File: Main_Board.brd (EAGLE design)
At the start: 160 x 100 mm, 50 parts, among them U1 RN4020RN4020, Y1 32KHz, Y2 25MHz

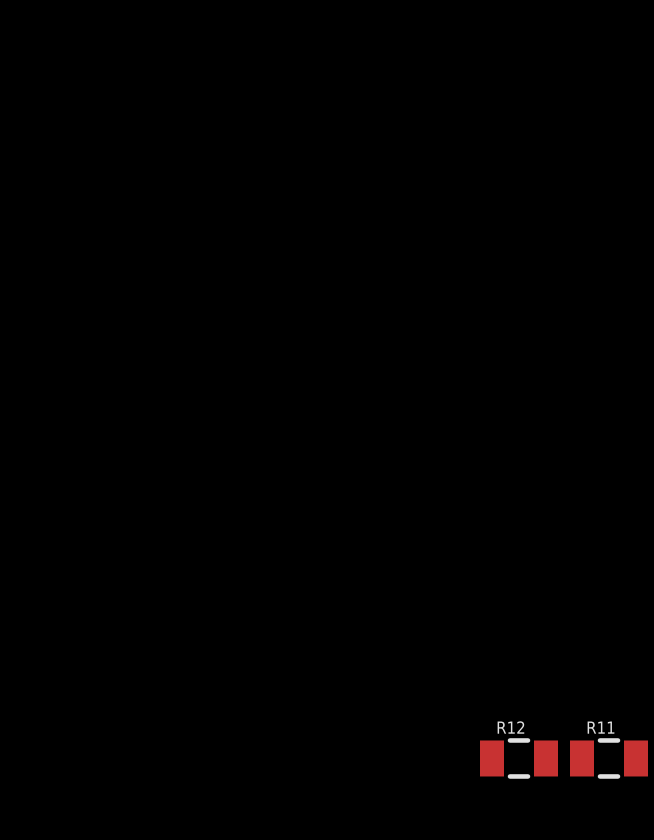
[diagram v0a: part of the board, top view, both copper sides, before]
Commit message: Added most remaining STM requirements
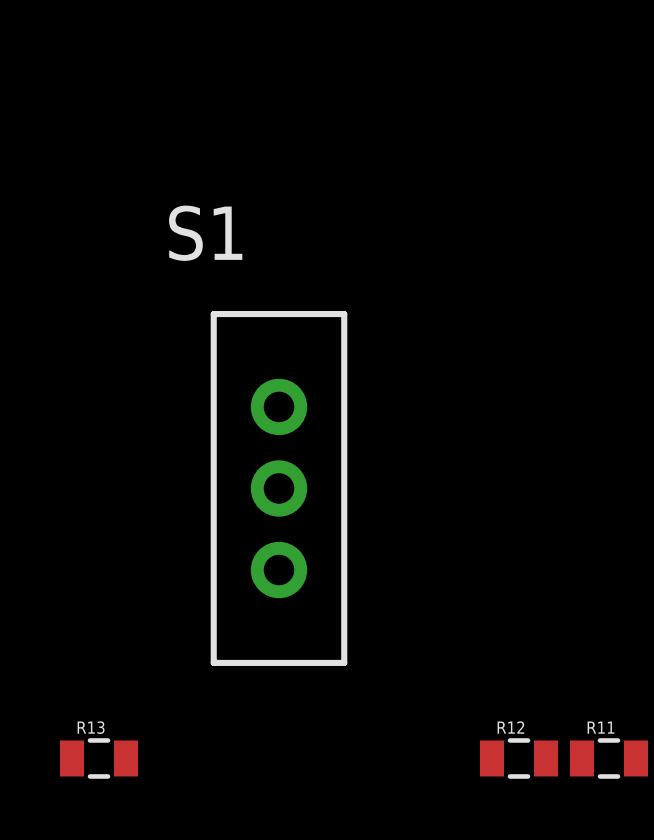
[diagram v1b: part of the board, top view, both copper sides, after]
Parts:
- added R13: 10K, SparkFun-Passives:0805
- added S1: (no value), SparkFun-Electromechanical:SWITCH-SPDT_LOCK.007S
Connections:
- new net N$22: R13.2, U$5.P$60
- new net N$23: R13.1, S1.2
- new net N$24: U$5.P$46
- new net N$25: U$5.P$49
- new net N$26: U$5.P$50
- new net N$27: U$5.P$55
- new net N$28: U$5.P$56
- net 3.3V: now also S1.3
- net GND: now also S1.1
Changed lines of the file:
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@@
 <element name="R11" library="SparkFun-Passives" package="0805" value="220" x="-171" y="-143"/>
 <element name="R12" library="SparkFun-Passives" package="0805" value="0" x="-174" y="-143"/>
+<element name="S1" library="SparkFun-Electromechanical" package="SWITCH-SPDT_LOCK.007S" value="" x="-182" y="-134"/>
+<element name="R13" library="SparkFun-Passives" package="0805" value="10K" x="-188" y="-143"/>
 </elements>
 <signals>
@@
 <contactref element="C20" pad="1"/>
 <contactref element="C19" pad="1"/>
+<contactref element="S1" pad="1"/>
 <wire x1="-125.05" y1="-132" x2="-123.1" y2="-132" width="0" layer="19" extent="1-1"/>
 <wire x1="-127" y1="-132" x2="-125.05" y2="-132" width="0" layer="19" extent="1-1"/>
@@
 <wire x1="-165.9" y1="-143" x2="-162.9" y2="-137" width="0" layer="19" extent="1-1"/>
 <wire x1="-168.9" y1="-143" x2="-165.9" y2="-143" width="0" layer="19" extent="1-1"/>
+<wire x1="-182" y1="-131.2822" x2="-168.9" y2="-143" width="0" layer="19" extent="1-1"/>
 <wire x1="-106.1" y1="-95" x2="-124.4" y2="-126.4" width="0" layer="19" extent="1-1"/>
 <wire x1="-103.1" y1="-95" x2="-106.1" y2="-95" width="0" layer="19" extent="1-1"/>
@@
 <contactref element="U1" pad="P$23"/>
 <contactref element="C15" pad="2"/>
+<contactref element="S1" pad="3"/>
 <wire x1="-121.9" y1="-131" x2="-127" y2="-126.4" width="0" layer="19" extent="1-1"/>
 <wire x1="-113" y1="-132" x2="-121.9" y2="-131" width="0" layer="19" extent="1-1"/>
@@
 <wire x1="-38.05" y1="-69.55" x2="-38.05" y2="-76.05" width="0" layer="19" extent="1-1"/>
 <wire x1="-47.55" y1="-67.55" x2="-49.55" y2="-77.05" width="0" layer="19" extent="1-1"/>
+<wire x1="-182" y1="-136.7178" x2="-135.1" y2="-131" width="0" layer="19" extent="1-1"/>
 </signal>
 <signal name="N$15">
@@
 <wire x1="-173.1" y1="-143" x2="-46.05" y2="-79.05" width="0" layer="19" extent="1-1"/>
 </signal>
+<signal name="N$22">
+<contactref element="R13" pad="2"/>
+<contactref element="U$5" pad="P$60"/>
+<wire x1="-187.1" y1="-143" x2="-49.55" y2="-75.05" width="0" layer="19" extent="1-1"/>
+</signal>
+<signal name="N$23">
+<contactref element="R13" pad="1"/>
+<contactref element="S1" pad="2"/>
+<wire x1="-182" y1="-134" x2="-188.9" y2="-143" width="0" layer="19" extent="1-1"/>
+</signal>
+<signal name="N$24">
+<contactref element="U$5" pad="P$46"/>
+</signal>
+<signal name="N$25">
+<contactref element="U$5" pad="P$49"/>
+</signal>
+<signal name="N$26">
+<contactref element="U$5" pad="P$50"/>
+</signal>
+<signal name="N$27">
+<contactref element="U$5" pad="P$55"/>
+</signal>
+<signal name="N$28">
+<contactref element="U$5" pad="P$56"/>
+</signal>
 </signals>

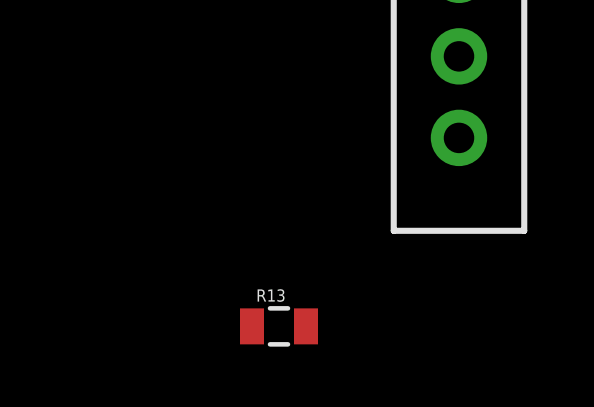
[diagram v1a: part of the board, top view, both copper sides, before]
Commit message: added extra oscillator resistor
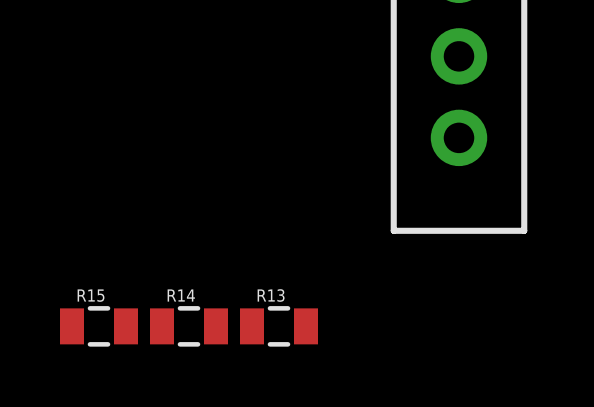
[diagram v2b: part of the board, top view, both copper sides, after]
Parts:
- added R14, R15: 0, SparkFun-Passives:0805
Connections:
- new net N$29: R14.2, U$5.P$3
- new net N$30: R15.2, U$5.P$5
- net N$12: now also R14.1; no longer U$5.P$3
- net N$20: now also R15.1; no longer U$5.P$5
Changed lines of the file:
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@@
 <element name="S1" library="SparkFun-Electromechanical" package="SWITCH-SPDT_LOCK.007S" value="" x="-182" y="-134"/>
 <element name="R13" library="SparkFun-Passives" package="0805" value="10K" x="-188" y="-143"/>
+<element name="R14" library="SparkFun-Passives" package="0805" value="0" x="-191" y="-143"/>
+<element name="R15" library="SparkFun-Passives" package="0805" value="0" x="-194" y="-143"/>
 </elements>
 <signals>
@@
 <signal name="N$12">
 <contactref element="Y1" pad="3"/>
-<contactref element="U$5" pad="P$3"/>
 <contactref element="C17" pad="2"/>
-<wire x1="-152.15" y1="-134.85" x2="-46.55" y2="-79.05" width="0" layer="19" extent="1-1"/>
-<wire x1="-158.1" y1="-137" x2="-152.15" y2="-134.85" width="0" layer="19" extent="1-1"/>
+<contactref element="R14" pad="1"/>
+<wire x1="-158.1" y1="-137" x2="-191.9" y2="-143" width="0" layer="19" extent="1-1"/>
+<wire x1="-152.15" y1="-134.85" x2="-158.1" y2="-137" width="0" layer="19" extent="1-1"/>
 </signal>
 <signal name="N$18">
@@
 <signal name="N$20">
 <contactref element="C20" pad="2"/>
-<contactref element="U$5" pad="P$5"/>
 <contactref element="Y2" pad="3"/>
-<wire x1="-158.15" y1="-140.85" x2="-45.55" y2="-79.05" width="0" layer="19" extent="1-1"/>
-<wire x1="-167.1" y1="-143" x2="-158.15" y2="-140.85" width="0" layer="19" extent="1-1"/>
+<contactref element="R15" pad="1"/>
+<wire x1="-167.1" y1="-143" x2="-194.9" y2="-143" width="0" layer="19" extent="1-1"/>
+<wire x1="-158.15" y1="-140.85" x2="-167.1" y2="-143" width="0" layer="19" extent="1-1"/>
 </signal>
 <signal name="N$21">
@@
 <contactref element="U$5" pad="P$56"/>
 </signal>
+<signal name="N$29">
+<contactref element="R14" pad="2"/>
+<contactref element="U$5" pad="P$3"/>
+<wire x1="-190.1" y1="-143" x2="-46.55" y2="-79.05" width="0" layer="19" extent="1-1"/>
+</signal>
+<signal name="N$30">
+<contactref element="U$5" pad="P$5"/>
+<contactref element="R15" pad="2"/>
+<wire x1="-193.1" y1="-143" x2="-45.55" y2="-79.05" width="0" layer="19" extent="1-1"/>
+</signal>
 </signals>

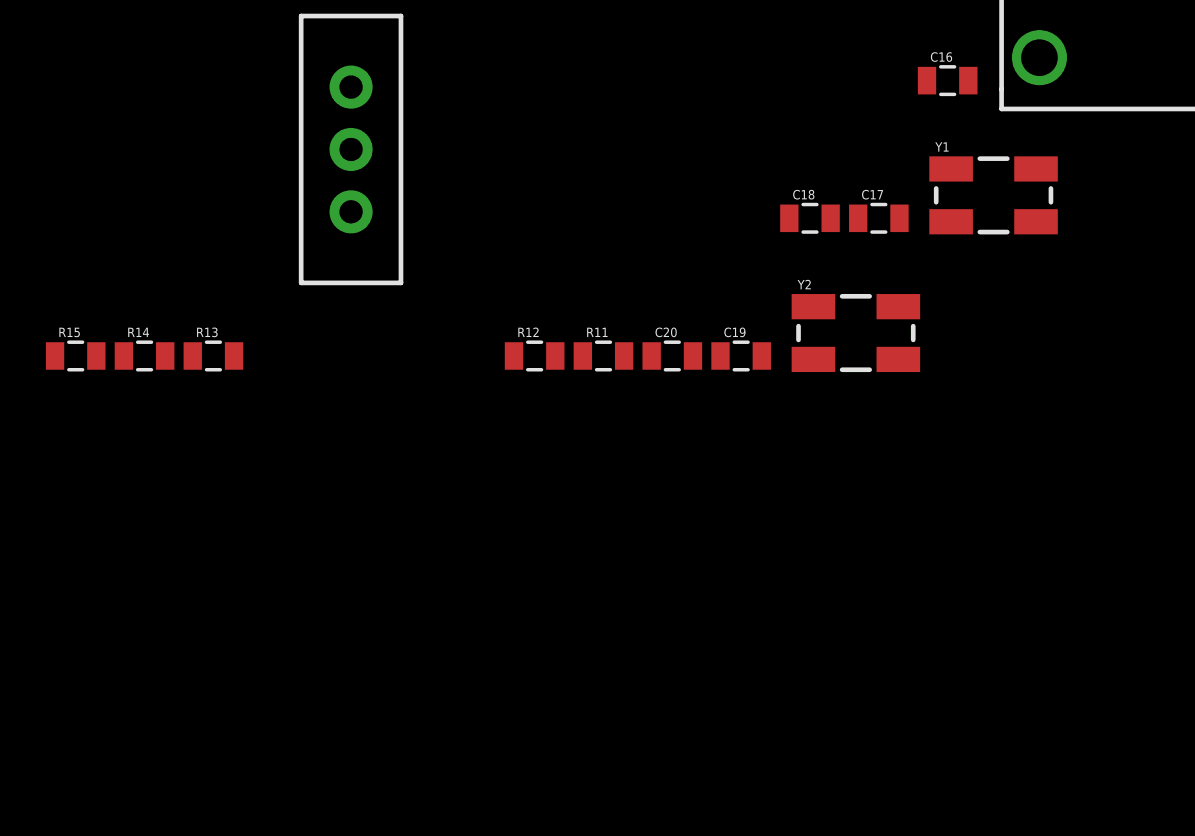
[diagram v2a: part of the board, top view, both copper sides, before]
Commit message: updated crystals
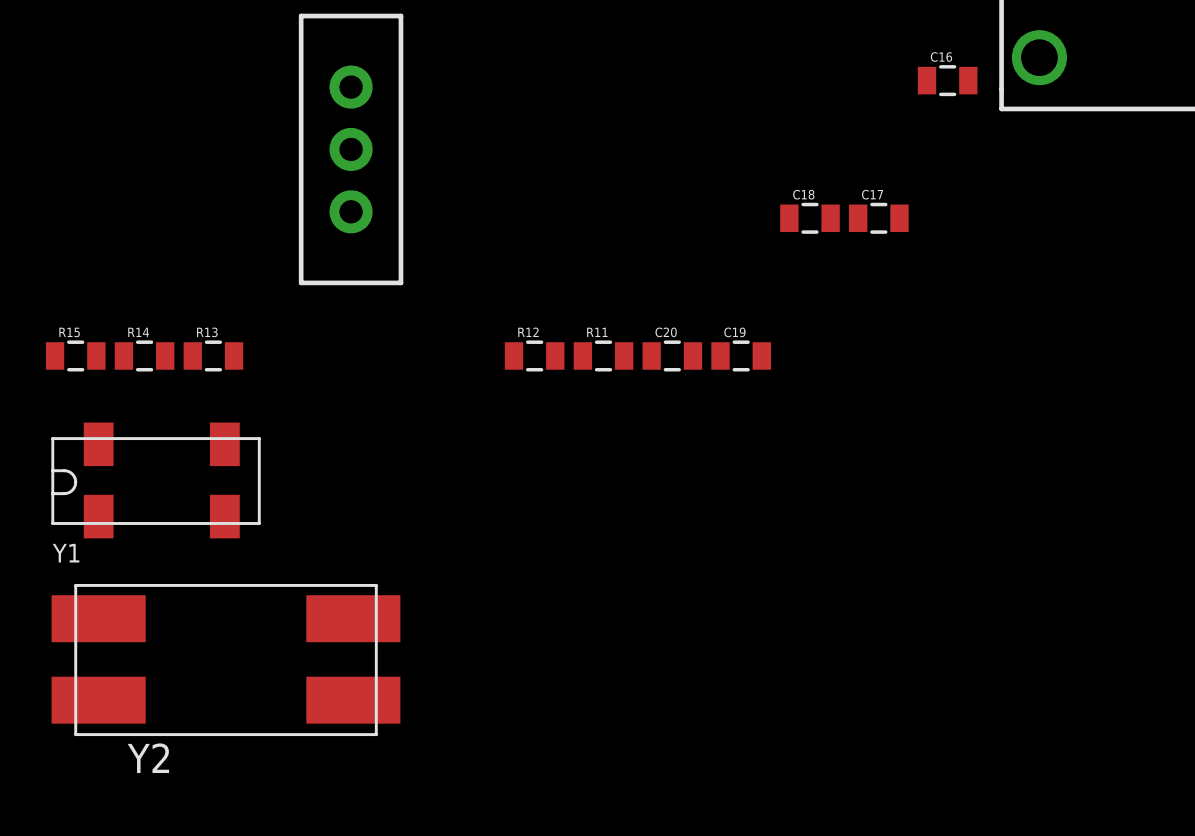
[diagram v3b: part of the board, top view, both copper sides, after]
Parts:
- Y1: value 32KHz -> MC-30632.768K-E3; device SparkFun-FreqCtrl:CRYSTAL-SMD-5X3 -> BB8:4-SMD,J-LEAD
- Y2: value 25MHz -> MA-5066-25.0000M-C0; device SparkFun-FreqCtrl:CRYSTAL-SMD-5X3 -> BB8:4-SMD,J-LEAD-2
- moved Y1 41.4 mm to (-193.0, -150.0)
- moved Y2 36.7 mm to (-193.0, -158.0)
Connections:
- net N$12: now also Y1.P$1; no longer Y1.3
- net N$17: now also Y2.P$4; no longer Y2.1
- net N$18: now also Y1.P$2; no longer Y1.1
- net N$20: now also Y2.P$1; no longer Y2.3
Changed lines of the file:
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@@
 <element name="U$11" library="SparkFun-Electromechanical" package="R_SW_TH" value="SWITCH-SPST-2RA" x="-152" y="-130"/>
 <element name="C16" library="SparkFun-Passives" package="0805" value=".1uF" x="-156" y="-131"/>
-<element name="Y1" library="SparkFun-FreqCtrl" package="CRYSTAL-SMD-5X3" value="32KHz" x="-154" y="-136">
-<attribute name="PROD_ID" value="XTAL-08297" x="-154" y="-136" size="1.778" layer="27" display="off"/>
-</element>
 <element name="C17" library="SparkFun-Passives" package="0805" value="6.8pF" x="-159" y="-137"/>
 <element name="C18" library="SparkFun-Passives" package="0805" value="6.8pF" x="-162" y="-137"/>
-<element name="Y2" library="SparkFun-FreqCtrl" package="CRYSTAL-SMD-5X3" value="25MHz" x="-160" y="-142">
-<attribute name="PROD_ID" value="XTAL-08297" x="-160" y="-142" size="1.778" layer="27" display="off"/>
-</element>
 <element name="C19" library="SparkFun-Passives" package="0805" value="20pF" x="-165" y="-143"/>
 <element name="C20" library="SparkFun-Passives" package="0805" value="20pF" x="-168" y="-143"/>
@@
 <element name="R14" library="SparkFun-Passives" package="0805" value="0" x="-191" y="-143"/>
 <element name="R15" library="SparkFun-Passives" package="0805" value="0" x="-194" y="-143"/>
+<element name="Y1" library="BB8" package="4-SMD,J-LEAD" value="MC-30632.768K-E3" x="-193" y="-150"/>
+<element name="Y2" library="BB8" package="4-SMD,J-LEAD-2" value="MA-5066-25.0000M-C0" x="-193" y="-158"/>
 </elements>
 <signals>
@@
 <contactref element="U$10" pad="P$9"/>
 <contactref element="C15" pad="1"/>
-<contactref element="C16" pad="2"/>
 <contactref element="U$11" pad="P$4"/>
 <contactref element="C16" pad="1"/>
+<contactref element="S1" pad="1"/>
 <contactref element="C17" pad="1"/>
 <contactref element="C18" pad="1"/>
 <contactref element="C20" pad="1"/>
 <contactref element="C19" pad="1"/>
-<contactref element="S1" pad="1"/>
+<contactref element="C16" pad="2"/>
 <wire x1="-125.05" y1="-132" x2="-123.1" y2="-132" width="0" layer="19" extent="1-1"/>
 <wire x1="-127" y1="-132" x2="-125.05" y2="-132" width="0" layer="19" extent="1-1"/>
@@
 <wire x1="-139.9096" y1="-114.506" x2="-44.55" y2="-79.05" width="0" layer="19" extent="1-1"/>
 </signal>
-<signal name="N$12">
-<contactref element="Y1" pad="3"/>
-<contactref element="C17" pad="2"/>
-<contactref element="R14" pad="1"/>
-<wire x1="-158.1" y1="-137" x2="-191.9" y2="-143" width="0" layer="19" extent="1-1"/>
-<wire x1="-152.15" y1="-134.85" x2="-158.1" y2="-137" width="0" layer="19" extent="1-1"/>
-</signal>
-<signal name="N$18">
-<contactref element="Y1" pad="1"/>
-<contactref element="C18" pad="2"/>
-<contactref element="R12" pad="1"/>
-<wire x1="-161.1" y1="-137" x2="-174.9" y2="-143" width="0" layer="19" extent="1-1"/>
-<wire x1="-155.85" y1="-137.15" x2="-161.1" y2="-137" width="0" layer="19" extent="1-1"/>
-</signal>
 <signal name="N$17">
 <contactref element="C19" pad="2"/>
-<contactref element="Y2" pad="1"/>
 <contactref element="R11" pad="1"/>
+<contactref element="Y2" pad="P$4"/>
+<wire x1="-171.9" y1="-143" x2="-193" y2="-154.45" width="0" layer="19" extent="1-1"/>
 <wire x1="-164.1" y1="-143" x2="-171.9" y2="-143" width="0" layer="19" extent="1-1"/>
-<wire x1="-161.85" y1="-143.15" x2="-164.1" y2="-143" width="0" layer="19" extent="1-1"/>
 </signal>
 <signal name="N$19">
@@
 <signal name="N$20">
 <contactref element="C20" pad="2"/>
-<contactref element="Y2" pad="3"/>
 <contactref element="R15" pad="1"/>
+<contactref element="Y2" pad="P$1"/>
+<wire x1="-194.9" y1="-143" x2="-193" y2="-158" width="0" layer="19" extent="1-1"/>
 <wire x1="-167.1" y1="-143" x2="-194.9" y2="-143" width="0" layer="19" extent="1-1"/>
-<wire x1="-158.15" y1="-140.85" x2="-167.1" y2="-143" width="0" layer="19" extent="1-1"/>
 </signal>
 <signal name="N$21">
@@
 <wire x1="-193.1" y1="-143" x2="-45.55" y2="-79.05" width="0" layer="19" extent="1-1"/>
 </signal>
+<signal name="N$18">
+<contactref element="C18" pad="2"/>
+<contactref element="R12" pad="1"/>
+<contactref element="Y1" pad="P$2"/>
+<wire x1="-174.9" y1="-143" x2="-187.5" y2="-150" width="0" layer="19" extent="1-1"/>
+<wire x1="-161.1" y1="-137" x2="-174.9" y2="-143" width="0" layer="19" extent="1-1"/>
+</signal>
+<signal name="N$12">
+<contactref element="C17" pad="2"/>
+<contactref element="Y1" pad="P$1"/>
+<contactref element="R14" pad="1"/>
+<wire x1="-191.9" y1="-143" x2="-193" y2="-150" width="0" layer="19" extent="1-1"/>
+<wire x1="-158.1" y1="-137" x2="-191.9" y2="-143" width="0" layer="19" extent="1-1"/>
+</signal>
 </signals>
